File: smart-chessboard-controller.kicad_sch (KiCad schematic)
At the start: 62 parts, among them J1 USB_C_Receptacle_USB2.0, J2 Micro_SD_Card_Det_Hirose_DM3C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, J3 Conn_02x03_Odd_Even, J4 Conn_01x12_MountingPin, J5 NX3224T024, J8 Conn_01x05, J9 Conn_01x05, Q1 S8050, Q2 S8050, SW2 SW_SPST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

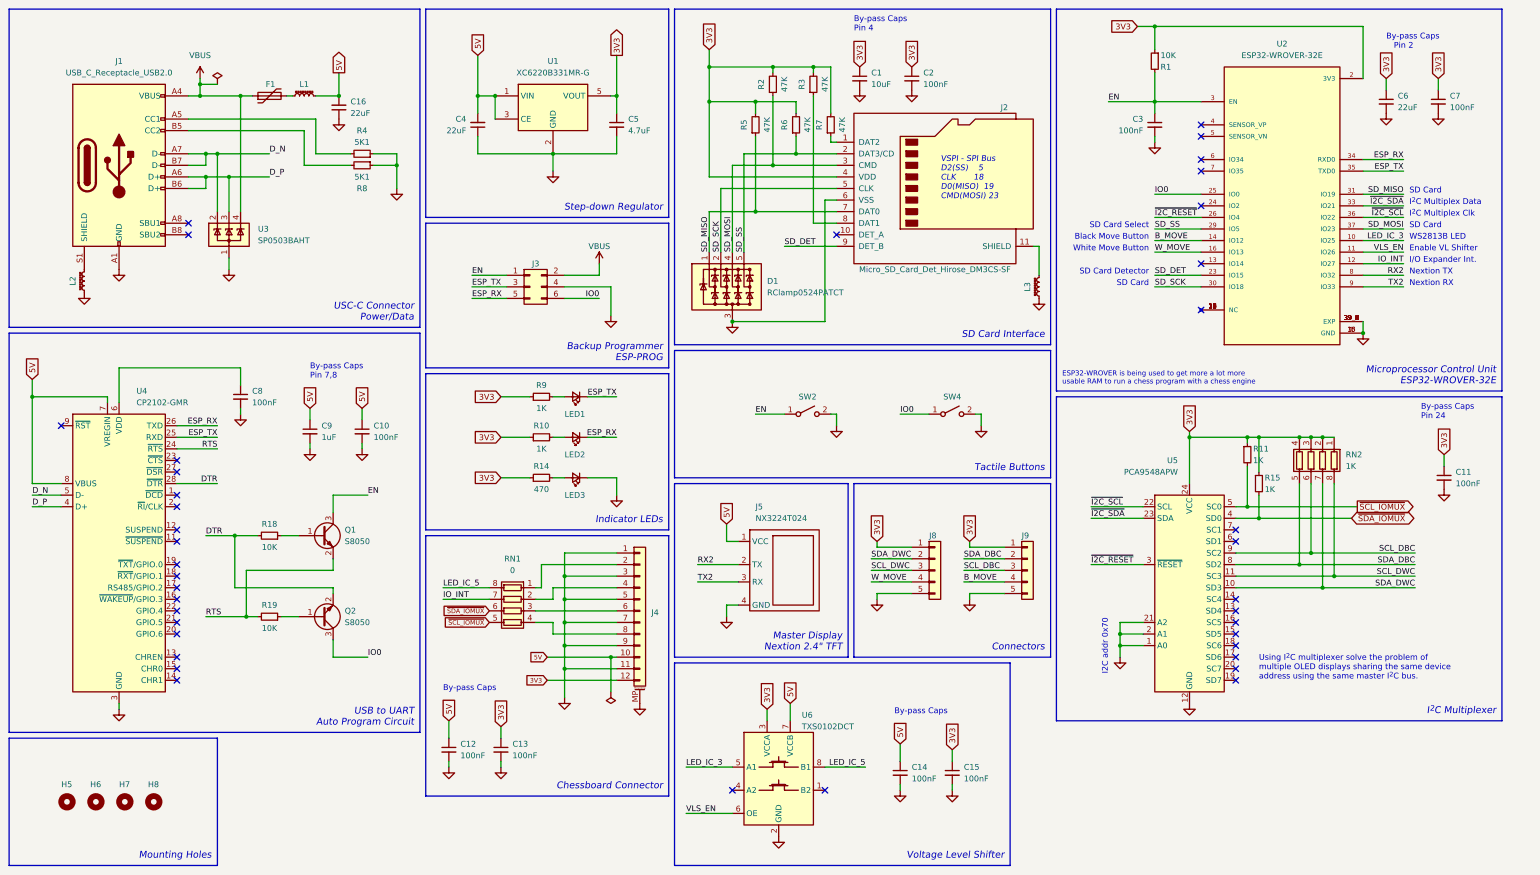
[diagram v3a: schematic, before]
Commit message: refactor schematic/pcb to add/remove components
- remove ESP programmer Tag Connect interface
- replace set of resistors to resistor array for SD card
- add pull-up resistors for interrupt and bus buffer enable pin
- tune trace length matching for data lines (i2c, ttl and spi)
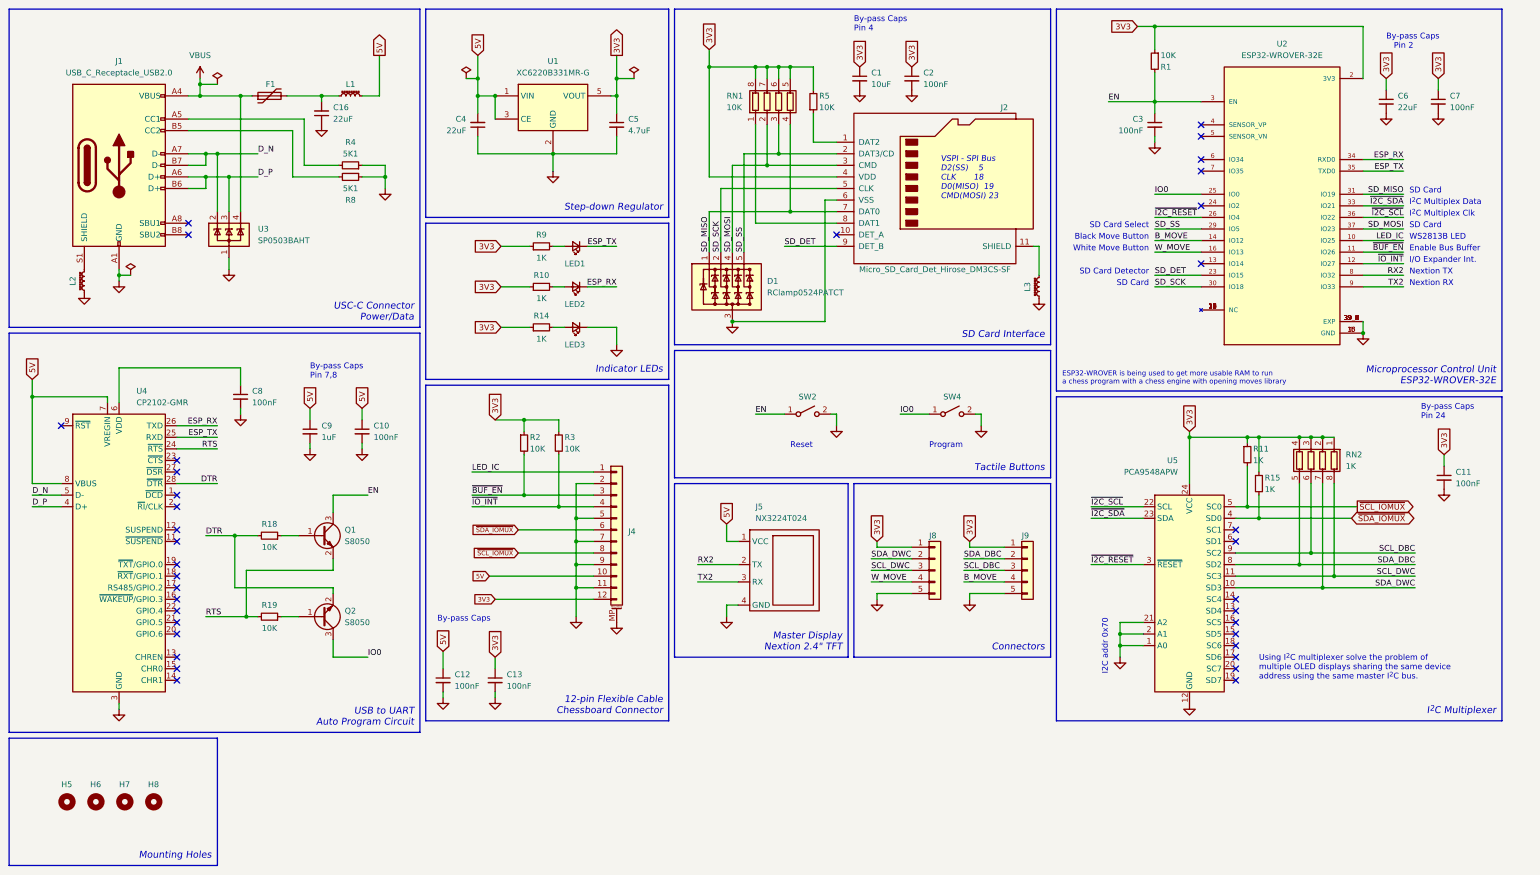
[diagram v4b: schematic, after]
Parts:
- removed C14, C15: 100nF, Capacitor_SMD:C_0603_1608Metric, symbol Device:C_Small
- removed J3: Conn_02x03_Odd_Even, Tag_Connect:TC2030-IDC-NL, symbol Connector_Generic:Conn_02x03_Odd_Even
- removed R6, R7: 47K, Resistor_SMD:R_0603_1608Metric, symbol Device:R_Small
- removed U6: TXS0102DCT, Package_SO:SSOP-8_2.95x2.8mm_P0.65mm, symbol Logic_LevelTranslator:TXS0102DCT
- F1: value C207047 -> BHFUSE BSMD1206-200-12V; footprint Fuse:Fuse_1210_3225Metric -> Fuse:Fuse_1206_3216Metric; LCSC C135353 -> C883135
- L1: footprint Inductor_SMD:L_0805_2012Metric_Pad1.15x1.40mm_HandSolder -> Inductor_SMD:L_0603_1608Metric; LCSC C61012 -> C62708
- R11, R15: LCSC (none) -> C21190
- R14: value 470 -> 1K; LCSC C23179 -> C21190
- R2, R3, R5: value 47K -> 10K; LCSC C25819 -> C25804
- RN1: value 0 -> 10K; LCSC (none) -> C29718
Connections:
- net LED_IC_5 is gone; now on net 3V3: RN1.8 (R1.2)
- net 3V3: now also R2.1, R3.1, RN1.5 (R4.2), RN1.6 (R3.2), RN1.7 (R2.2); no longer R2.2, R3.2
- net 5V: no longer C16.2
- net GND: now also J4.2 (Pin_2); no longer J4.1 (Pin_1), J4.3 (Pin_3)
- net SD_MISO: now also RN1.4 (R4.1); no longer R5.1
- net SD_MOSI: now also RN1.2 (R2.1); no longer R2.1
- net SD_SS: now also RN1.3 (R3.1)
- net ~{SCL_IOMUX}: now also J4.8 (Pin_8); no longer RN1.5 (R4.2)
- net ~{SDA_IOMUX}: now also J4.6 (Pin_6); no longer RN1.6 (R3.2)
- net at RN1.1 (R1.1): now also J2.8 (DAT1); no longer J4.2 (Pin_2)
- net ~{IO_INT}: now reaches J4.4 (Pin_4)
- net ~{IO_INT}: now also R3.2, U2.12 (IO27); no longer RN1.2 (R2.1)
- net at F1.2, L1.1: now also C16.2
- net at J2.1 (DAT2): now also R5.1
- removed net IO_INT: RN1.7 (R2.2), U2.12 (IO27)
- net LED_IC_3 renamed LED_IC
- net LED_IC: now also J4.1 (Pin_1)
- net VLS_EN renamed ~{BUF_EN}
- net ~{BUF_EN}: now also J4.3 (Pin_3), R2.2
- no-connect marks 39 -> 36
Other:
- note added: "12-pin Flexible Cable Chessboard Connector"
- note added: "ESP32-WROVER is being used to get more usable RAM to run a chess program with a chess engine with opening moves library"
- note added: "Enable Bus Buffer"
- note added: "Program"
- note added: "Reset"
- note removed: "Backup Programmer ESP-PROG"
- note removed: "Chessboard Connector"
- note removed: "ESP32-WROVER is being used to get more a lot more usable RAM to run a chess program with a chess engine"
- note removed: "Enable VL Shifter"
- note removed: "Voltage Level Shifter"
- moved on the sheet: C12, C13, C16, J4, L1, LED1, LED2, LED3, R10, R14, R4, R5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

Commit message: update manufacturing files
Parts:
- L2, L3: LCSC C113018 -> C62708
- U2: value ESP32-WROVER-32E -> ESP32-WROVER-E-N8R8; LCSC C2973667 -> C701348
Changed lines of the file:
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@@
     (in_bom yes) (on_board yes) (fields_autoplaced)
     (property "Reference" "U2" (id 0) (at 293.37 21.59 0))
-    (property "Value" "ESP32-WROVER-32E" (id 1) (at 293.37 24.13 0))
+    (property "Value" "ESP32-WROVER-E-N8R8" (id 1) (at 293.37 24.13 0))
     (property "Footprint" "User Custom Footprint:XCVR_ESP32-WROVER-E-N4R8" (id 2) (at 293.37 57.15 0)
       (effects (font (size 1.27 1.27)) (justify bottom) hide)
     )
-    (property "Datasheet" "https://datasheet.lcsc.com/lcsc/2207151200_Espressif-Systems-ESP32-WROVER-E-N8R8_C2973667.pdf" (id 3) (at 293.37 57.15 0)
-      (effects (font (size 1.27 1.27)) hide)
-    )
-    (property "LCSC" " C2973667" (id 4) (at 293.37 57.15 0)
+    (property "Datasheet" "https://www.espressif.com/sites/default/files/documentation/esp32-wrover-e_esp32-wrover-ie_datasheet_en.pdf" (id 3) (at 293.37 57.15 0)
+      (effects (font (size 1.27 1.27)) hide)
+    )
+    (property "LCSC" "C701348" (id 4) (at 293.37 57.15 0)
       (effects (font (size 1.27 1.27)) hide)
     )
@@
       (effects (font (size 1.27 1.27)) hide)
     )
-    (property "LCSC" "C113018" (id 4) (at 30.48 73.66 0)
+    (property "LCSC" "C62708" (id 4) (at 30.48 73.66 0)
       (effects (font (size 1.27 1.27)) hide)
     )
@@
       (effects (font (size 1.27 1.27)) hide)
     )
-    (property "LCSC" "C113018" (id 4) (at 240.03 74.93 0)
+    (property "LCSC" "C62708" (id 4) (at 240.03 74.93 0)
       (effects (font (size 1.27 1.27)) hide)
     )
@@
     )
     (path "/7531744a-adfd-462a-a28f-135299bc08b0"
-      (reference "U2") (unit 1) (value "ESP32-WROVER-32E") (footprint "User Custom Footprint:XCVR_ESP32-WROVER-E-N4R8")
+      (reference "U2") (unit 1) (value "ESP32-WROVER-E-N8R8") (footprint "User Custom Footprint:XCVR_ESP32-WROVER-E-N4R8")
     )
     (path "/bbc54aa5-5efc-46ea-83fa-f9acfbcc058f"

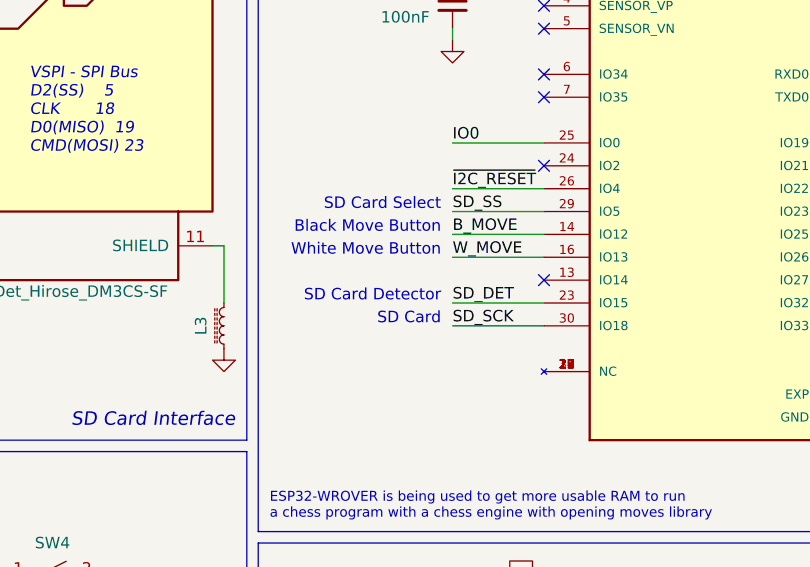
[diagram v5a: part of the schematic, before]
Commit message: update SD card detect pin assignment
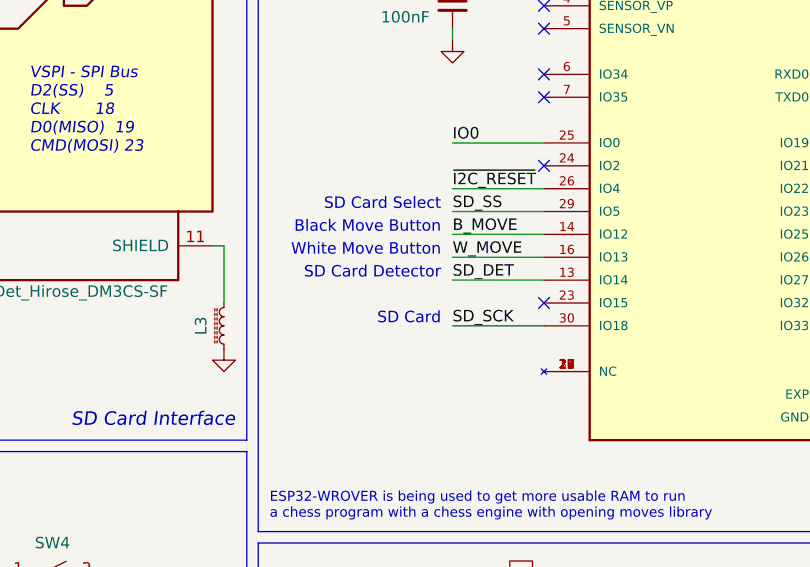
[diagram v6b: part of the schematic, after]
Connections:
- net SD_DET: now also U2.13 (IO14); no longer U2.23 (IO15)
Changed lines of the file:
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@@
   (no_connect (at 275.59 39.37))
   (no_connect (at 283.21 128.27))
-  (no_connect (at 275.59 69.85))
+  (no_connect (at 275.59 72.39))
   (no_connect (at 283.21 151.13))
   (no_connect (at 283.21 143.51))
@@
     (stroke (width 0) (type default) (color 0 0 0 0))
   )
-  (wire (pts (xy 265.43 72.39) (xy 275.59 72.39))
+  (wire (pts (xy 265.43 69.85) (xy 275.59 69.85))
     (stroke (width 0) (type default) (color 0 0 0 0))
   )
@@
     (effects (font (size 1.27 1.27)) (justify left bottom))
   )
-  (text "SD Card Detector" (at 264.16 72.39 180)
+  (text "SD Card Detector" (at 264.16 69.85 180)
     (effects (font (size 1.27 1.27)) (justify right bottom))
   )
@@
     (effects (font (size 1.27 1.27)) (justify left bottom))
   )
-  (label "SD_DET" (at 265.43 72.39 0)
-    (effects (font (size 1.27 1.27)) (justify left bottom))
-  )
+  (label "SD_DET" (at 265.43 69.85 0)
+    (effects (font (size 1.27 1.27)) (justify left bottom))
+  )

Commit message: replace USB-C part that was out of stock
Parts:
- J1: LCSC C167321 -> C2982555
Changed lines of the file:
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@@
       (effects (font (size 1.27 1.27)) hide)
     )
-    (property "LCSC" "C167321" (id 4) (at 38.1 48.26 0)
+    (property "LCSC" "C2982555" (id 4) (at 38.1 48.26 0)
       (effects (font (size 1.27 1.27)) hide)
     )
